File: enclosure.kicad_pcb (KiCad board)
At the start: 2 copper layers, 100 x 220 mm, 3 parts

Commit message: add full-bridge sub layout
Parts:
- added C1001: 470u, enclosure:CP_Elec_10x10, F.Cu at (123.3, 77.4)
- added C1002: 1u, enclosure:C_0603_1608Metric_Pad1.08x0.95mm_HandSolder, F.Cu at (129.8, 92.9)
- added C1003: 1u, enclosure:C_0603_1608Metric_Pad1.08x0.95mm_HandSolder, F.Cu at (129.8, 95.4)
- added C1004: 10u, enclosure:C_1210_3225Metric_Pad1.33x2.70mm_HandSolder, F.Cu at (133.1, 73.6)
- added C1005: 10u, enclosure:C_1210_3225Metric_Pad1.33x2.70mm_HandSolder, F.Cu at (133.1, 77.8)
- added C101: 100n, enclosure:C_0805_2012Metric_Pad1.18x1.45mm_HandSolder, F.Cu at (0.68, 130.9)
- added C201: 10u, enclosure:C_1210_3225Metric_Pad1.33x2.70mm_HandSolder, F.Cu at (75.8, 100.4)
- added C202: 470p, enclosure:C_0805_2012Metric_Pad1.18x1.45mm_HandSolder, F.Cu at (70.4, 75.9)
- added C203: 100n, enclosure:C_0805_2012Metric_Pad1.18x1.45mm_HandSolder, F.Cu at (70.4, 78.9)
- added C204: 100n, enclosure:C_0805_2012Metric_Pad1.18x1.45mm_HandSolder, F.Cu at (70.4, 81.9)
- added C205: 100n, enclosure:C_0805_2012Metric_Pad1.18x1.45mm_HandSolder, F.Cu at (70.4, 84.9)
- added C206: 10u, enclosure:C_1210_3225Metric_Pad1.33x2.70mm_HandSolder, F.Cu at (75.8, 104.6)
- added C207: 100n, enclosure:C_0805_2012Metric_Pad1.18x1.45mm_HandSolder, F.Cu at (70.4, 87.9)
- added C208: 470p, enclosure:C_0805_2012Metric_Pad1.18x1.45mm_HandSolder, F.Cu at (70.4, 90.9)
- added C209: 470p, enclosure:C_0805_2012Metric_Pad1.18x1.45mm_HandSolder, F.Cu at (70.4, 93.9)
- added C210: 470p, enclosure:C_0805_2012Metric_Pad1.18x1.45mm_HandSolder, F.Cu at (70.4, 96.9)
- added C301: 100n, enclosure:C_0805_2012Metric_Pad1.18x1.45mm_HandSolder, F.Cu at (86.2, 124.9)
- added C302: 470p, enclosure:C_0805_2012Metric_Pad1.18x1.45mm_HandSolder, F.Cu at (86.2, 127.9)
- added C303: 470p, enclosure:C_0805_2012Metric_Pad1.18x1.45mm_HandSolder, F.Cu at (86.2, 130.9)
- added C304: 100n, enclosure:C_0805_2012Metric_Pad1.18x1.45mm_HandSolder, F.Cu at (86.2, 133.9)
- added C305: 100n, enclosure:C_0805_2012Metric_Pad1.18x1.45mm_HandSolder, F.Cu at (86.2, 136.9)
- added C306: 10u, enclosure:C_1210_3225Metric_Pad1.33x2.70mm_HandSolder, F.Cu at (79.1, 140.8)
- added C401: 100n, enclosure:C_0805_2012Metric_Pad1.18x1.45mm_HandSolder, F.Cu at (190.9, 102.0)
- added C501: 100n, enclosure:C_0805_2012Metric_Pad1.18x1.45mm_HandSolder, F.Cu at (242.4, 102.2)
- added C601: 100n, enclosure:C_0805_2012Metric_Pad1.18x1.45mm_HandSolder, F.Cu at (216.9, 102.7)
- added C701: 470u, enclosure:CP_Elec_10x10, F.Cu at (190.5, 75.2)
- added C702: 100n, enclosure:C_0805_2012Metric_Pad1.18x1.45mm_HandSolder, F.Cu at (181.6, 81.6)
- added C801: 470u, enclosure:CP_Elec_10x10, F.Cu at (215.9, 75.2)
- added C802: 100n, enclosure:C_0805_2012Metric_Pad1.18x1.45mm_HandSolder, F.Cu at (207.0, 81.6)
- added C901: 470u, enclosure:CP_Elec_10x10, F.Cu at (241.3, 75.2)
- added C902: 100n, enclosure:C_0805_2012Metric_Pad1.18x1.45mm_HandSolder, F.Cu at (232.4, 81.6)
- added D1001: D_TVS, enclosure:D_SOD-323_HandSoldering, F.Cu at (134.5, 93.1)
- added D1002: 1N4148, enclosure:D_SOD-123, F.Cu at (111.2, 81.2)
- added D1003: 1N4148, enclosure:D_SOD-123, F.Cu at (111.2, 84.5)
- added D1004: 1N4148, enclosure:D_SOD-123, F.Cu at (111.2, 87.9)
- added D201: D_TVS, enclosure:D_SOD-323_HandSoldering, F.Cu at (96.0, 96.9)
- added D202: D_TVS, enclosure:D_SOD-323_HandSoldering, F.Cu at (96.0, 99.8)
- added D203: D_TVS, enclosure:D_SOD-323_HandSoldering, F.Cu at (96.0, 102.8)
- added D204: D_TVS, enclosure:D_SOD-323_HandSoldering, F.Cu at (96.0, 105.7)
- added D205: PDZ5.6B115, enclosure:D_SOD-323_HandSoldering, F.Cu at (96.0, 108.7)
- added D701: D_TVS, enclosure:D_SOD-323_HandSoldering, F.Cu at (179.0, 70.1)
- added D801: D_TVS, enclosure:D_SOD-323_HandSoldering, F.Cu at (204.4, 70.1)
- added D901: D_TVS, enclosure:D_SOD-323_HandSoldering, F.Cu at (229.8, 70.1)
- added F1002: Fuse_Socket, enclosure:FuseHolder_Blade_ATO_Littelfuse_FLR_178.6165, F.Cu at (205.2, 48.6)
- added J101: Conn_01x06_Socket, enclosure:PhoenixContact_TDPT_2,5_6-SP-5,08_1x06_P5.08mm_Horizontal, F.Cu at (182.7, 61.2)
- added J102: Conn_01x02_Socket, enclosure:PhoenixContact_TDPT_2,5_2-SP-5,08_1x02_P5.08mm_Horizontal, F.Cu at (195.0, 61.2)
- added J103: Conn_01x02_Socket, enclosure:PhoenixContact_TDPT_2,5_2-SP-5,08_1x02_P5.08mm_Horizontal, F.Cu at (242.6, 61.2)
- added J104: Conn_01x02_Socket, enclosure:PhoenixContact_TDPT_2,5_2-SP-5,08_1x02_P5.08mm_Horizontal, F.Cu at (230.0, 61.2)
- added J105: Conn_01x02_Socket, enclosure:PhoenixContact_TDPT_2,5_2-SP-5,08_1x02_P5.08mm_Horizontal, F.Cu at (217.5, 61.2)
- added JP1001: SolderJumper_2_Open, enclosure:SolderJumper-2_P1.3mm_Open_RoundedPad1.0x1.5mm, F.Cu at (106.1, 81.3)
- added JP1002: SolderJumper_2_Open, enclosure:SolderJumper-2_P1.3mm_Open_RoundedPad1.0x1.5mm, F.Cu at (106.1, 84.8)
- added JP1003: SolderJumper_2_Open, enclosure:SolderJumper-2_P1.3mm_Open_RoundedPad1.0x1.5mm, F.Cu at (106.1, 88.4)
- added JP1004: SolderJumper_2_Open, enclosure:SolderJumper-2_P1.3mm_Open_RoundedPad1.0x1.5mm, F.Cu at (106.1, 92.0)
- added JP101: SolderJumper_3_Bridged12, enclosure:SolderJumper-3_P1.3mm_Bridged12-Soldermask-Paste_RoundedPad1.0x1.5mm, F.Cu at (-4.55, 131.2)
- added JP102: SolderJumper_3_Bridged12, enclosure:SolderJumper-3_P1.3mm_Bridged12-Soldermask-Paste_RoundedPad1.0x1.5mm, F.Cu at (-4.55, 135.0)
- added JP103: SolderJumper_2_Open, enclosure:SolderJumper-2_P1.3mm_Open_RoundedPad1.0x1.5mm, F.Cu at (19.2, 111.7)
- added JP104: SolderJumper_2_Open, enclosure:SolderJumper-2_P1.3mm_Open_RoundedPad1.0x1.5mm, F.Cu at (19.2, 115.2)
- added JP105: SolderJumper_2_Open, enclosure:SolderJumper-2_P1.3mm_Open_RoundedPad1.0x1.5mm, F.Cu at (19.2, 118.8)
- added JP106: SolderJumper_2_Open, enclosure:SolderJumper-2_P1.3mm_Open_RoundedPad1.0x1.5mm, F.Cu at (19.2, 122.3)
- added JP107: SolderJumper_2_Open, enclosure:SolderJumper-2_P1.3mm_Open_RoundedPad1.0x1.5mm, F.Cu at (19.2, 125.9)
- added JP108: SolderJumper_2_Open, enclosure:SolderJumper-2_P1.3mm_Open_RoundedPad1.0x1.5mm, F.Cu at (19.2, 129.4)
- added JP109: SolderJumper_2_Open, enclosure:SolderJumper-2_P1.3mm_Open_RoundedPad1.0x1.5mm, F.Cu at (19.2, 133.0)
- added JP110: SolderJumper_2_Open, enclosure:SolderJumper-2_P1.3mm_Open_RoundedPad1.0x1.5mm, F.Cu at (23.6, 111.7)
- added JP111: SolderJumper_2_Open, enclosure:SolderJumper-2_P1.3mm_Open_RoundedPad1.0x1.5mm, F.Cu at (23.6, 115.2)
- added JP112: SolderJumper_2_Open, enclosure:SolderJumper-2_P1.3mm_Open_RoundedPad1.0x1.5mm, F.Cu at (23.6, 118.8)
- added JP113: SolderJumper_2_Open, enclosure:SolderJumper-2_P1.3mm_Open_RoundedPad1.0x1.5mm, F.Cu at (23.6, 122.3)
- added JP114: SolderJumper_2_Open, enclosure:SolderJumper-2_P1.3mm_Open_RoundedPad1.0x1.5mm, F.Cu at (23.6, 125.9)
- added JP115: SolderJumper_2_Open, enclosure:SolderJumper-2_P1.3mm_Open_RoundedPad1.0x1.5mm, F.Cu at (23.6, 129.4)
- added JP116: SolderJumper_2_Open, enclosure:SolderJumper-2_P1.3mm_Open_RoundedPad1.0x1.5mm, F.Cu at (23.6, 133.0)
- added JP117: SolderJumper_2_Open, enclosure:SolderJumper-2_P1.3mm_Open_RoundedPad1.0x1.5mm, F.Cu at (27.9, 111.7)
- added JP118: SolderJumper_2_Open, enclosure:SolderJumper-2_P1.3mm_Open_RoundedPad1.0x1.5mm, F.Cu at (27.9, 115.2)
- added JP119: SolderJumper_2_Open, enclosure:SolderJumper-2_P1.3mm_Open_RoundedPad1.0x1.5mm, F.Cu at (27.9, 118.8)
- added JP120: SolderJumper_2_Open, enclosure:SolderJumper-2_P1.3mm_Open_RoundedPad1.0x1.5mm, F.Cu at (27.9, 122.3)
- added JP121: SolderJumper_2_Open, enclosure:SolderJumper-2_P1.3mm_Open_RoundedPad1.0x1.5mm, F.Cu at (27.9, 125.9)
- added JP122: SolderJumper_2_Open, enclosure:SolderJumper-2_P1.3mm_Open_RoundedPad1.0x1.5mm, F.Cu at (27.9, 129.4)
- added JP123: SolderJumper_2_Open, enclosure:SolderJumper-2_P1.3mm_Open_RoundedPad1.0x1.5mm, F.Cu at (27.9, 133.0)
- added JP301: SolderJumper_3_Bridged12, enclosure:SolderJumper-3_P1.3mm_Bridged12-Soldermask-Paste_RoundedPad1.0x1.5mm, F.Cu at (78.9, 144.7)
- added JP701: SolderJumper_3_Bridged12, enclosure:SolderJumper-3_P1.3mm_Bridged12-Soldermask-Paste_RoundedPad1.0x1.5mm, F.Cu at (193.7, 92.4)
- added JP801: SolderJumper_3_Bridged12, enclosure:SolderJumper-3_P1.3mm_Bridged12-Soldermask-Paste_RoundedPad1.0x1.5mm, F.Cu at (219.1, 92.4)
- added JP901: SolderJumper_3_Bridged12, enclosure:SolderJumper-3_P1.3mm_Bridged12-Soldermask-Paste_RoundedPad1.0x1.5mm, F.Cu at (244.4, 92.4)
- added Q1001: DPLS350E, enclosure:SOT-223-3_TabPin2, F.Cu at (132.5, 87.5)
- added R1001: 5R9, enclosure:R_1210_3225Metric_Pad1.30x2.65mm_HandSolder, F.Cu at (111.2, 91.7)
- added R201: 330, enclosure:R_1210_3225Metric_Pad1.30x2.65mm_HandSolder, F.Cu at (88.7, 76.5)
- added R202: 1M, enclosure:R_1210_3225Metric_Pad1.30x2.65mm_HandSolder, F.Cu at (88.7, 80.7)
- added R203: 1M, enclosure:R_1210_3225Metric_Pad1.30x2.65mm_HandSolder, F.Cu at (88.7, 84.9)
- added R204: 1M, enclosure:R_1210_3225Metric_Pad1.30x2.65mm_HandSolder, F.Cu at (88.7, 89.1)
- added R205: 100, enclosure:R_1210_3225Metric_Pad1.30x2.65mm_HandSolder, F.Cu at (88.7, 93.3)
- added R206: 1M, enclosure:R_1210_3225Metric_Pad1.30x2.65mm_HandSolder, F.Cu at (94.6, 76.5)
- added R207: 1M, enclosure:R_1210_3225Metric_Pad1.30x2.65mm_HandSolder, F.Cu at (94.6, 80.7)
- added R208: 100, enclosure:R_1210_3225Metric_Pad1.30x2.65mm_HandSolder, F.Cu at (94.6, 84.9)
- added R209: 100, enclosure:R_1210_3225Metric_Pad1.30x2.65mm_HandSolder, F.Cu at (94.6, 89.1)
- added R210: 100, enclosure:R_1210_3225Metric_Pad1.30x2.65mm_HandSolder, F.Cu at (94.6, 93.3)
- added R301: 100, enclosure:R_1210_3225Metric_Pad1.30x2.65mm_HandSolder, F.Cu at (91.6, 125.5)
- added R302: 100, enclosure:R_1210_3225Metric_Pad1.30x2.65mm_HandSolder, F.Cu at (91.6, 129.7)
- added R401: 1M, enclosure:R_1210_3225Metric_Pad1.30x2.65mm_HandSolder, F.Cu at (177.7, 107.4)
- added R402: 280k, enclosure:R_1210_3225Metric_Pad1.30x2.65mm_HandSolder, F.Cu at (181.9, 107.4)
- added R403: 10k, enclosure:R_1210_3225Metric_Pad1.30x2.65mm_HandSolder, F.Cu at (186.1, 107.4)
- added R404: 2k49, enclosure:R_1210_3225Metric_Pad1.30x2.65mm_HandSolder, F.Cu at (190.3, 107.4)
- added R405: 100k, enclosure:R_1210_3225Metric_Pad1.30x2.65mm_HandSolder, F.Cu at (194.6, 107.4)
- added R501: 1M, enclosure:R_1210_3225Metric_Pad1.30x2.65mm_HandSolder, F.Cu at (229.2, 107.6)
- added R502: 280k, enclosure:R_1210_3225Metric_Pad1.30x2.65mm_HandSolder, F.Cu at (233.4, 107.6)
- added R503: 10k, enclosure:R_1210_3225Metric_Pad1.30x2.65mm_HandSolder, F.Cu at (237.6, 107.6)
- added R504: 2k49, enclosure:R_1210_3225Metric_Pad1.30x2.65mm_HandSolder, F.Cu at (241.8, 107.6)
- added R505: 100k, enclosure:R_1210_3225Metric_Pad1.30x2.65mm_HandSolder, F.Cu at (246.1, 107.6)
- added R601: 1M, enclosure:R_1210_3225Metric_Pad1.30x2.65mm_HandSolder, F.Cu at (203.8, 108.1)
- added R602: 280k, enclosure:R_1210_3225Metric_Pad1.30x2.65mm_HandSolder, F.Cu at (208.0, 108.1)
- added R603: 10k, enclosure:R_1210_3225Metric_Pad1.30x2.65mm_HandSolder, F.Cu at (212.2, 108.1)
- added R604: 2k49, enclosure:R_1210_3225Metric_Pad1.30x2.65mm_HandSolder, F.Cu at (216.4, 108.1)
- added R605: 100k, enclosure:R_1210_3225Metric_Pad1.30x2.65mm_HandSolder, F.Cu at (220.6, 108.1)
- added R701: 1M, enclosure:R_1210_3225Metric_Pad1.30x2.65mm_HandSolder, F.Cu at (178.4, 93.6)
- added R702: 1M, enclosure:R_1210_3225Metric_Pad1.30x2.65mm_HandSolder, F.Cu at (182.2, 93.6)
- added R703: 1M, enclosure:R_1210_3225Metric_Pad1.30x2.65mm_HandSolder, F.Cu at (186.0, 93.6)
- added R704: 1k, enclosure:R_1210_3225Metric_Pad1.30x2.65mm_HandSolder, F.Cu at (178.4, 87.9)
- added R705: 1k, enclosure:R_1210_3225Metric_Pad1.30x2.65mm_HandSolder, F.Cu at (182.2, 87.9)
- added R706: 1k, enclosure:R_1210_3225Metric_Pad1.30x2.65mm_HandSolder, F.Cu at (186.0, 87.9)
- added R707: 1k, enclosure:R_1210_3225Metric_Pad1.30x2.65mm_HandSolder, F.Cu at (193.7, 87.9)
- added R708: 1k, enclosure:R_1210_3225Metric_Pad1.30x2.65mm_HandSolder, F.Cu at (189.8, 87.9)
- added R709: 10k, enclosure:R_1210_3225Metric_Pad1.30x2.65mm_HandSolder, F.Cu at (177.1, 81.6)
- added R801: 1M, enclosure:R_1210_3225Metric_Pad1.30x2.65mm_HandSolder, F.Cu at (203.8, 93.6)
- added R802: 1M, enclosure:R_1210_3225Metric_Pad1.30x2.65mm_HandSolder, F.Cu at (207.6, 93.6)
- added R803: 1M, enclosure:R_1210_3225Metric_Pad1.30x2.65mm_HandSolder, F.Cu at (211.4, 93.6)
- added R804: 1k, enclosure:R_1210_3225Metric_Pad1.30x2.65mm_HandSolder, F.Cu at (203.8, 87.9)
- added R805: 1k, enclosure:R_1210_3225Metric_Pad1.30x2.65mm_HandSolder, F.Cu at (207.6, 87.9)
- added R806: 1k, enclosure:R_1210_3225Metric_Pad1.30x2.65mm_HandSolder, F.Cu at (211.4, 87.9)
- added R807: 1k, enclosure:R_1210_3225Metric_Pad1.30x2.65mm_HandSolder, F.Cu at (219.1, 87.9)
- added R808: 1k, enclosure:R_1210_3225Metric_Pad1.30x2.65mm_HandSolder, F.Cu at (215.2, 87.9)
- added R809: 10k, enclosure:R_1210_3225Metric_Pad1.30x2.65mm_HandSolder, F.Cu at (202.5, 81.6)
- added R901: 1M, enclosure:R_1210_3225Metric_Pad1.30x2.65mm_HandSolder, F.Cu at (229.2, 93.6)
- added R902: 1M, enclosure:R_1210_3225Metric_Pad1.30x2.65mm_HandSolder, F.Cu at (233.0, 93.6)
- added R903: 1M, enclosure:R_1210_3225Metric_Pad1.30x2.65mm_HandSolder, F.Cu at (236.8, 93.6)
- added R904: 1k, enclosure:R_1210_3225Metric_Pad1.30x2.65mm_HandSolder, F.Cu at (229.2, 87.9)
- added R905: 1k, enclosure:R_1210_3225Metric_Pad1.30x2.65mm_HandSolder, F.Cu at (233.0, 87.9)
- added R906: 1k, enclosure:R_1210_3225Metric_Pad1.30x2.65mm_HandSolder, F.Cu at (236.8, 87.9)
- added R907: 1k, enclosure:R_1210_3225Metric_Pad1.30x2.65mm_HandSolder, F.Cu at (244.4, 87.9)
- added R908: 1k, enclosure:R_1210_3225Metric_Pad1.30x2.65mm_HandSolder, F.Cu at (240.6, 87.9)
- added R909: 10k, enclosure:R_1210_3225Metric_Pad1.30x2.65mm_HandSolder, F.Cu at (227.9, 81.6)
- added TP1001: ~, enclosure:TP_0805_2012Metric, F.Cu at (118.0, 84.8)
- added TP1002: ~, enclosure:TP_0805_2012Metric, F.Cu at (118.0, 87.9)
- added TP1003: ~, enclosure:TP_0805_2012Metric, F.Cu at (118.0, 90.9)
- added TP1004: ~, enclosure:TP_0805_2012Metric, F.Cu at (121.8, 84.8)
- added TP1005: ~, enclosure:TP_0805_2012Metric, F.Cu at (121.8, 87.9)
- added TP1006: ~, enclosure:TP_0805_2012Metric, F.Cu at (121.8, 90.9)
- added TP1007: ~, enclosure:TP_0805_2012Metric, F.Cu at (125.7, 84.8)
- added TP1008: ~, enclosure:TP_0805_2012Metric, F.Cu at (125.7, 87.9)
- added TP1009: ~, enclosure:TP_0805_2012Metric, F.Cu at (125.7, 90.9)
- added TP201: ~, enclosure:TP_0805_2012Metric, F.Cu at (87.6, 96.9)
- added TP202: ~, enclosure:TP_0805_2012Metric, F.Cu at (87.6, 100.0)
- added TP203: ~, enclosure:TP_0805_2012Metric, F.Cu at (87.6, 103.0)
- added TP204: ~, enclosure:TP_0805_2012Metric, F.Cu at (87.6, 106.1)
- added TP205: ~, enclosure:TP_0805_2012Metric, F.Cu at (87.6, 109.1)
- added TP206: ~, enclosure:TP_0805_2012Metric, F.Cu at (91.5, 96.9)
- added TP207: ~, enclosure:TP_0805_2012Metric, F.Cu at (91.5, 100.0)
- added TP208: ~, enclosure:TP_0805_2012Metric, F.Cu at (91.5, 103.0)
- added TP209: ~, enclosure:TP_0805_2012Metric, F.Cu at (91.5, 106.1)
- added TP210: ~, enclosure:TP_0805_2012Metric, F.Cu at (91.5, 109.1)
- added TP301: ~, enclosure:TP_0805_2012Metric, F.Cu at (78.0, 124.9)
- added TP302: ~, enclosure:TP_0805_2012Metric, F.Cu at (78.0, 128.0)
- added TP303: ~, enclosure:TP_0805_2012Metric, F.Cu at (78.0, 131.0)
- added TP304: ~, enclosure:TP_0805_2012Metric, F.Cu at (78.0, 134.1)
- added TP305: ~, enclosure:TP_0805_2012Metric, F.Cu at (78.0, 137.1)
- added TP306: ~, enclosure:TP_0805_2012Metric, F.Cu at (81.9, 124.9)
- added TP307: ~, enclosure:TP_0805_2012Metric, F.Cu at (81.9, 128.0)
- added TP308: ~, enclosure:TP_0805_2012Metric, F.Cu at (81.9, 131.0)
- added TP401: ~, enclosure:TP_0805_2012Metric, F.Cu at (177.1, 102.5)
- added TP402: ~, enclosure:TP_0805_2012Metric, F.Cu at (180.2, 102.5)
- added TP403: ~, enclosure:TP_0805_2012Metric, F.Cu at (183.2, 102.5)
- added TP501: ~, enclosure:TP_0805_2012Metric, F.Cu at (228.6, 102.7)
- added TP502: ~, enclosure:TP_0805_2012Metric, F.Cu at (231.7, 102.7)
- added TP503: ~, enclosure:TP_0805_2012Metric, F.Cu at (234.7, 102.7)
- added TP601: ~, enclosure:TP_0805_2012Metric, F.Cu at (203.2, 103.2)
- added TP602: ~, enclosure:TP_0805_2012Metric, F.Cu at (206.2, 103.2)
- added TP603: ~, enclosure:TP_0805_2012Metric, F.Cu at (209.3, 103.2)
- added U1001: MC7805, enclosure:TO-252-2, F.Cu at (110.8, 67.4)
- added U1002: MC7812, enclosure:TO-252-2, F.Cu at (110.8, 75.5)
- added U101: 4041, enclosure:SOIC-14_3.9x8.7mm_P1.27mm, F.Cu at (-11.6, 134.7)
- added U201: Si8641BD-B-IS2, enclosure:SOIC-16W_7.5x10.3mm_P1.27mm, F.Cu at (79.2, 80.4)
- added U202: R05C05TE05S, enclosure:SOIC-16W_7.5x10.3mm_P1.27mm, F.Cu at (79.2, 92.3)
- added U301: SN74LVC1G04DBVR, enclosure:SOT-23-5_HandSoldering, F.Cu at (91.5, 134.3)
- added U302: AD567xR, enclosure:TSSOP-20_4.4x6.5mm_P0.65mm, F.Cu at (88.5, 142.5)
- added U401: LTC6992IS6-1, enclosure:TSOT-23-6, F.Cu at (187.2, 101.9)
- added U501: LTC6992IS6-1, enclosure:TSOT-23-6, F.Cu at (238.7, 102.0)
- added U601: LTC6992IS6-1, enclosure:TSOT-23-6, F.Cu at (213.2, 102.5)
- added U701: VNH7070ASTR, enclosure:SO-16_3.9x9.9mm_P1.27mm, F.Cu at (179.0, 75.2)
- added U801: VNH7070ASTR, enclosure:SO-16_3.9x9.9mm_P1.27mm, F.Cu at (204.4, 75.2)
- added U901: VNH7070ASTR, enclosure:SO-16_3.9x9.9mm_P1.27mm, F.Cu at (229.8, 75.2)
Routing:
- net GND: track 0.00 -> 188.5 mm, vias 0 -> 114
- net +24V: track 0.00 -> 36.3 mm, vias 0 -> 56
- net Net-(U901-CS): track 0.00 -> 34.7 mm, vias 0 -> 2
- net Net-(U801-CS): track 0.00 -> 34.7 mm, vias 0 -> 2
- net Net-(U701-CS): track 0.00 -> 34.7 mm, vias 0 -> 2
- net Net-(U901-PWM): track 0.00 -> 33.6 mm, vias 0 -> 2
- net Net-(U801-PWM): track 0.00 -> 33.6 mm, vias 0 -> 2
- net Net-(U701-PWM): track 0.00 -> 33.6 mm, vias 0 -> 2
- net Net-(U801-SEL0): track 0.00 -> 32.9 mm, vias 0 -> 2
- net Net-(U701-SEL0): track 0.00 -> 32.9 mm, vias 0 -> 2
- net Net-(U901-SEL0): track 0.00 -> 32.9 mm, vias 0 -> 2
- net +5VA_full-bridge: track 0.00 -> 19.0 mm, vias 0 -> 3
- net +12VA: track 0.00 -> 18.1 mm, vias 0 -> 28
- net Net-(U701-IN_B): track 0.00 -> 16.1 mm, vias 0 -> 2
- net Net-(U801-IN_B): track 0.00 -> 16.1 mm, vias 0 -> 2
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- added copper zone on B.Cu, net +12VA
- added copper zone on F.Cu, net +12VA
- added copper zone on B.Cu, net +24V
- added copper zone on F.Cu, net +24V
- added copper zone on B.Cu, net +5VA_full-bridge
- added copper zone on F.Cu, net /fan_+
- added copper zone on F.Cu, net /fan_-
- added copper zone on F.Cu, net /heater_+
- added copper zone on F.Cu, net /heater_-
- added copper zone on F.Cu, net /peltier_+
- added copper zone on F.Cu, net /peltier_-
- added copper zone on B.Cu, net GND
- added copper zone on F.Cu, net GND

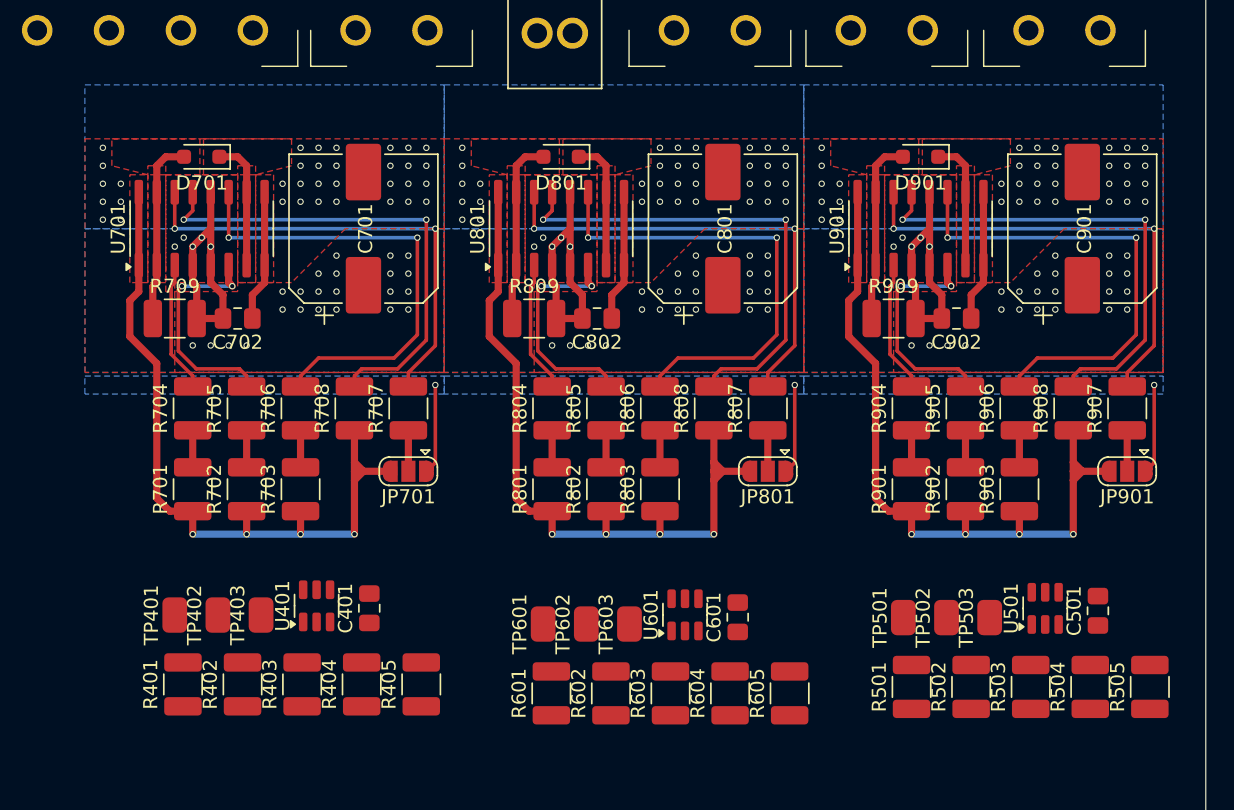
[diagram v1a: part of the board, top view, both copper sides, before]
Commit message: add pwm sub layout
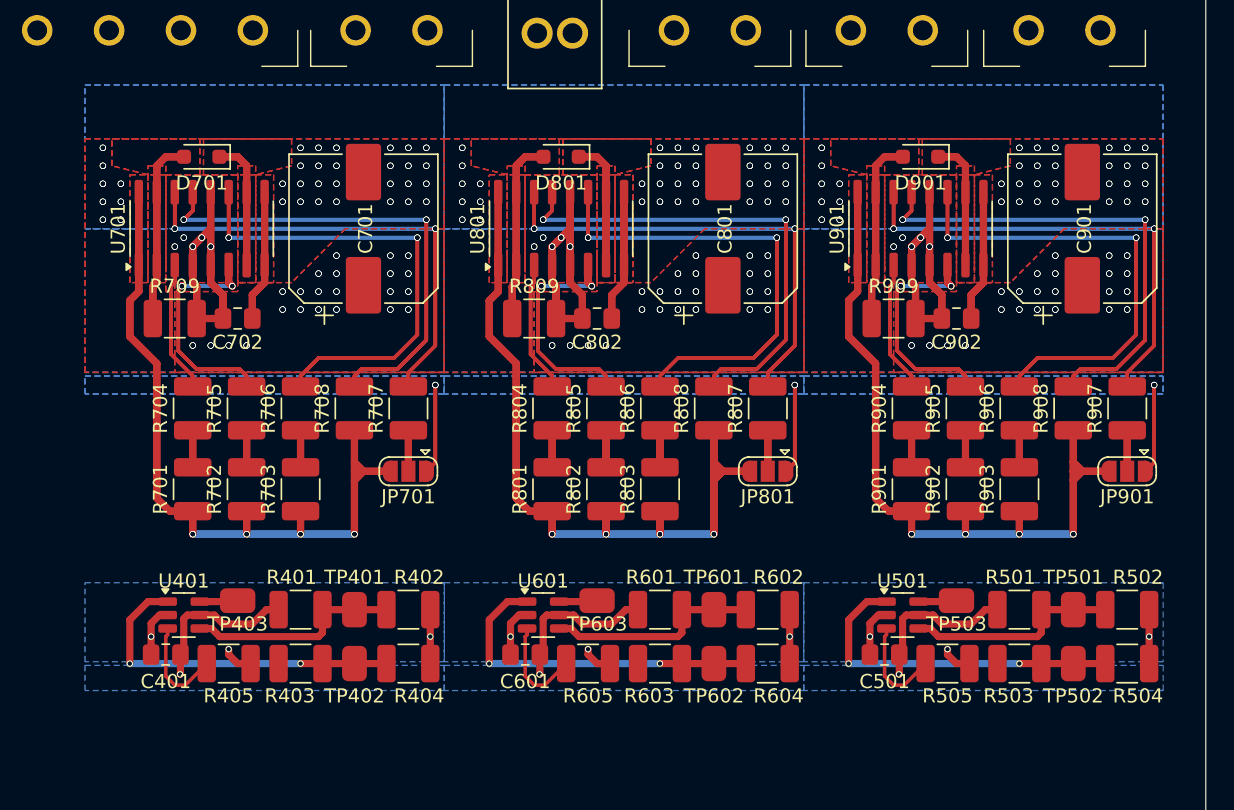
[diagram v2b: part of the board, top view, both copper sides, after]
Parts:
- moved C501 15.4 mm to (227.3, 105.3), turned to 0 degrees
- moved C601 15.3 mm to (201.9, 105.3), turned to 0 degrees
- moved C401 14.8 mm to (176.5, 105.3), turned to 0 degrees
- moved R605 14.4 mm to (206.3, 105.9), turned to 180 degrees
- moved R505 14.4 mm to (231.8, 105.9), turned to 180 degrees
- moved R405 13.7 mm to (180.9, 105.9), turned to 180 degrees
- moved R402 12.9 mm to (193.7, 102.1), turned to 180 degrees
- moved TP401 12.7 mm to (189.8, 102.1)
- moved R602 12.6 mm to (219.1, 102.1), turned to 180 degrees
- moved R502 12.3 mm to (244.4, 102.1), turned to 180 degrees
- moved TP601 12.1 mm to (215.2, 102.1)
- moved TP501 12.0 mm to (240.6, 102.1)
- moved TP402 10.2 mm to (189.8, 105.9)
- moved U501 10.1 mm to (228.6, 102.5), turned to 0 degrees
- moved U601 10.0 mm to (203.2, 102.5), turned to 0 degrees
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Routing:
- net GND: track 188.5 -> 405.8 mm, vias 114 -> 237
- net +24V: track 36.3 -> 72.5 mm, vias 56 -> 112
- net Net-(U901-CS): track 34.7 -> 69.5 mm, vias 2 -> 4
- net Net-(U801-CS): track 34.7 -> 69.5 mm, vias 2 -> 4
- net Net-(U701-CS): track 34.7 -> 69.5 mm, vias 2 -> 4
- net +5VA_pwm: track 0.00 -> 34.6 mm, vias 0 -> 3
- net Net-(U901-PWM): track 33.6 -> 67.2 mm, vias 2 -> 4
- net Net-(U801-PWM): track 33.6 -> 67.2 mm, vias 2 -> 4
- net Net-(U701-PWM): track 33.6 -> 67.2 mm, vias 2 -> 4
- net Net-(U801-SEL0): track 32.9 -> 65.9 mm, vias 2 -> 4
- net Net-(U701-SEL0): track 32.9 -> 65.9 mm, vias 2 -> 4
- net Net-(U901-SEL0): track 32.9 -> 65.9 mm, vias 2 -> 4
- net /dac_ch_1: track 0.00 -> 24.4 mm, vias 0 -> 2
- net /dac_ch_2: track 0.00 -> 24.4 mm, vias 0 -> 2
- net /dac_ch_0: track 0.00 -> 24.4 mm, vias 0 -> 2
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- added copper zone on F.Cu, net +5VA_full-bridge
- added copper zone on B.Cu, net +5VA_pwm
- added copper zone on B.Cu, net /fan_+
- added copper zone on B.Cu, net /heater_+
- added copper zone on B.Cu, net /peltier_+
- added copper zone on B.Cu, net /pwm1/div
- added copper zone on B.Cu, net /pwm2/div

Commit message: ajust output channel order
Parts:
- moved JP104 222.4 mm to (240.6, 94.9), turned to 90 degrees
- moved JP103 196.8 mm to (215.2, 94.9), turned to 90 degrees
- moved JP105 172.3 mm to (189.8, 94.9), turned to 90 degrees
- moved C901 50.8 mm to (190.5, 75.2)
- moved D901 50.8 mm to (179.0, 70.1)
- moved R901 50.8 mm to (178.4, 93.6)
- moved R902 50.8 mm to (182.2, 93.6)
- moved R903 50.8 mm to (186.0, 93.6)
- moved R904 50.8 mm to (178.4, 87.9)
- moved R905 50.8 mm to (182.2, 87.9)
- moved R906 50.8 mm to (186.0, 87.9)
- moved R909 50.8 mm to (177.1, 81.6)
- moved U901 50.8 mm to (179.0, 75.2)
- moved C902 50.8 mm to (181.6, 81.6)
- moved JP901 50.8 mm to (193.7, 92.4)
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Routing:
- net GND: track 405.8 -> 156.3 mm
- net +24V: track 72.5 -> 36.3 mm
- net Net-(U901-CS): track 69.5 -> 34.7 mm
- net Net-(U701-CS): track 69.5 -> 34.7 mm
- net Net-(U801-CS): track 69.5 -> 34.7 mm
- net Net-(U901-PWM): track 67.2 -> 33.6 mm
- net Net-(U801-PWM): track 67.2 -> 33.6 mm
- net Net-(U701-PWM): track 67.2 -> 33.6 mm
- net Net-(U801-SEL0): track 65.9 -> 32.9 mm
- net Net-(U701-SEL0): track 65.9 -> 32.9 mm
- net Net-(U901-SEL0): track 65.9 -> 32.9 mm
- net /fan_+: track 26.2 -> 54.9 mm
- net /fan_-: track 18.4 -> 37.5 mm
- net +5VA_full-bridge: track 38.1 -> 19.0 mm
- net +12VA: track 36.3 -> 18.1 mm
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- removed copper zone on B.Cu, net /fan_+
- removed copper zone on B.Cu, net /heater_+
- removed copper zone on B.Cu, net /pwm2/div

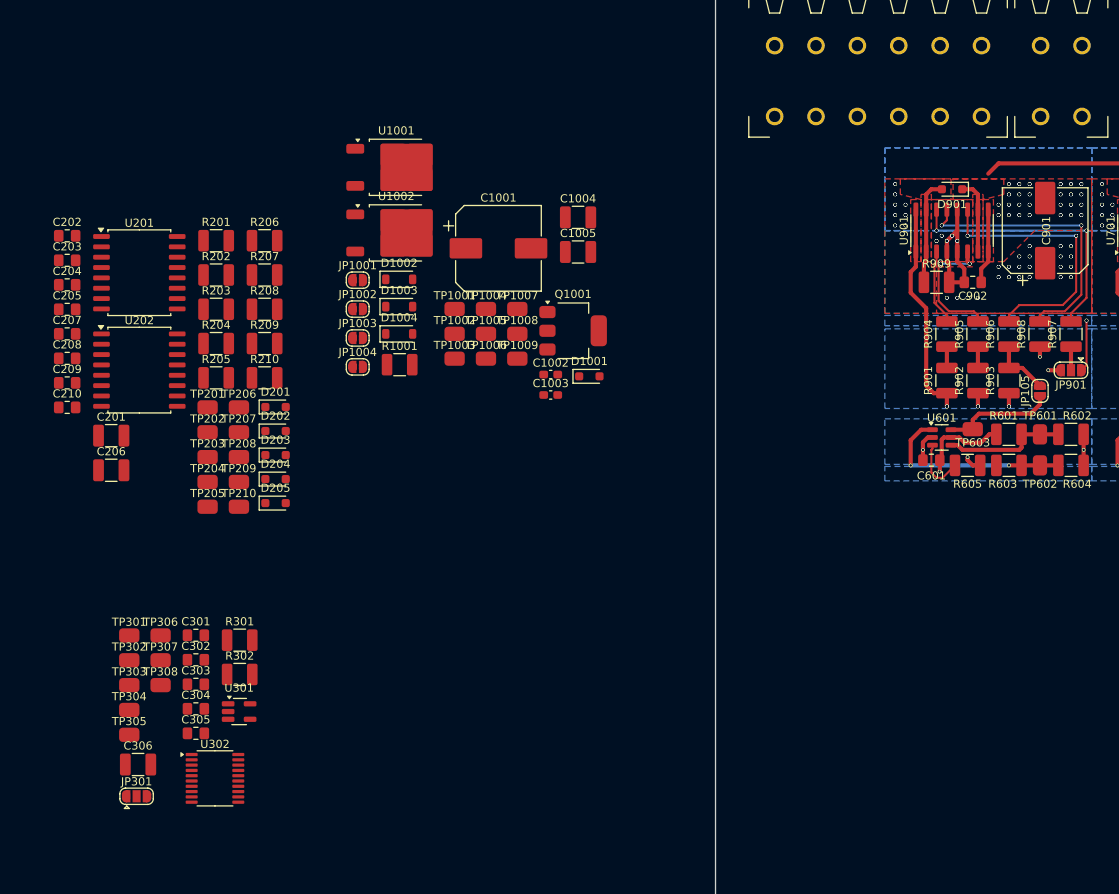
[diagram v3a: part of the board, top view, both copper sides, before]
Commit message: add digital-interface sub layout
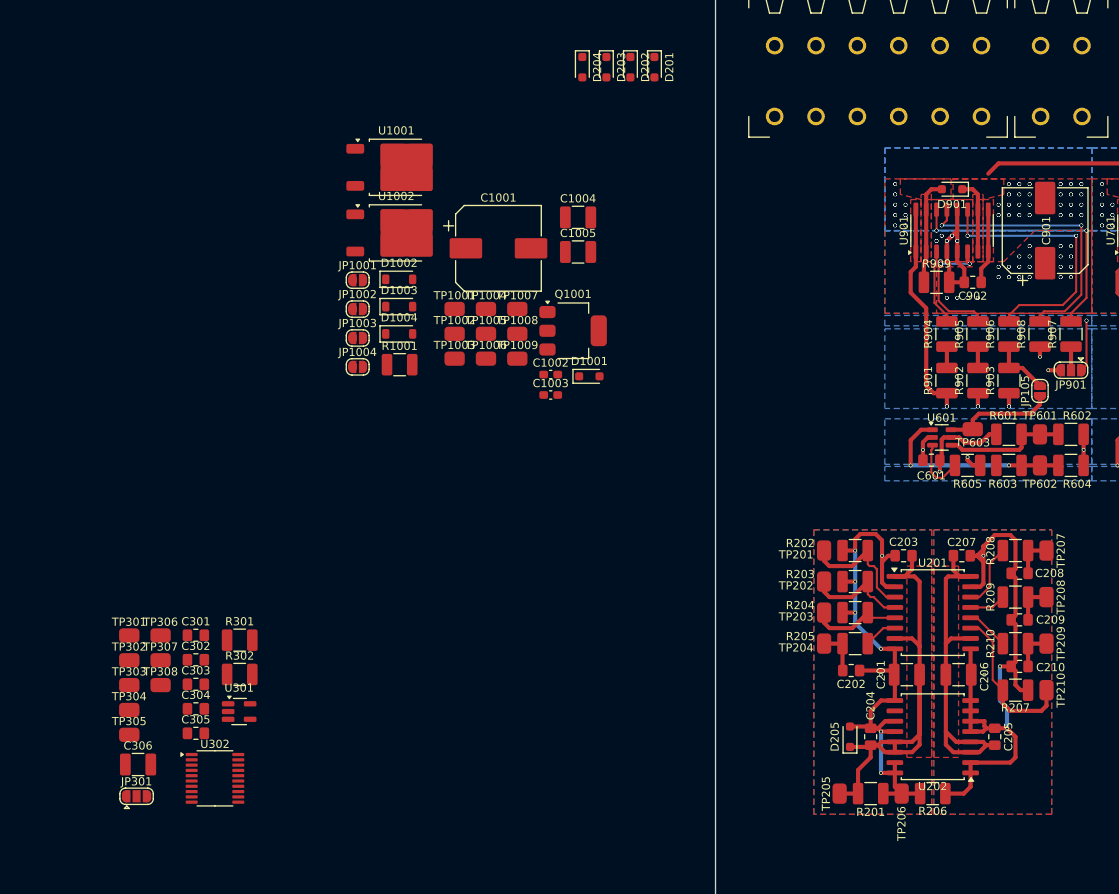
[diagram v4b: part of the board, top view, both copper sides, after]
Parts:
- moved C205 125.4 mm to (184.3, 137.4), turned to -90 degrees
- moved C210 121.2 mm to (187.3, 128.7)
- moved C209 120.5 mm to (187.3, 123.0)
- moved C208 119.9 mm to (187.3, 117.3)
- moved C204 113.2 mm to (169.1, 137.4), turned to -90 degrees
- moved C207 113.2 mm to (180.2, 115.1), turned to 180 degrees
- moved C202 110.1 mm to (166.7, 129.2), turned to 180 degrees
- moved C203 108.9 mm to (173.1, 115.1)
- moved U202 107.3 mm to (176.7, 137.4), turned to 180 degrees
- moved C206 107.0 mm to (179.8, 129.7), turned to 180 degrees
- moved R206 106.5 mm to (176.7, 144.3)
- moved U201 106.0 mm to (176.7, 122.1)
- moved R207 105.4 mm to (186.8, 131.6), turned to 180 degrees
- moved R201 105.2 mm to (169.1, 144.3), turned to 180 degrees
- moved C201 102.0 mm to (173.5, 129.7)
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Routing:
- net GND: track 156.3 -> 235.5 mm, vias 237 -> 241
- net GNDI: track 0.00 -> 73.4 mm, vias 0 -> 8
- net +5VI: track 0.00 -> 63.5 mm
- net +5VA_digital-interface: track 0.00 -> 43.4 mm
- net /digital-interface/SDO: track 0.00 -> 19.4 mm
- net /digital-interface/~{CS_ISO}: track 0.00 -> 15.7 mm
- net /digital-interface/SCKL_ISO: track 0.00 -> 13.2 mm
- net /digital-interface/SDI_ISO: track 0.00 -> 11.3 mm
- net Net-(U201-B1): track 0.00 -> 7.98 mm
- net /digital-interface/SDO_ISO: track 0.00 -> 5.57 mm
- net Net-(U201-B3): track 0.00 -> 5.28 mm
- net /digital-interface/~{CS}: track 0.00 -> 5.06 mm
- net /digital-interface/SDI: track 0.00 -> 5.06 mm
- net /digital-interface/SCKL: track 0.00 -> 5.06 mm
- net Net-(U201-A4): track 0.00 -> 4.52 mm
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- added copper zone on B.Cu, net +5VI
- added copper zone on F.Cu, net +5VI
- added copper zone on B.Cu, net /digital-interface/SDI
- added copper zone on F.Cu, net /digital-interface/SDI
- added copper zone on F.Cu, net GNDI
